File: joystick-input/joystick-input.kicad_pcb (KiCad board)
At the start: 2 copper layers, 53.3 x 39.4 mm, 11 parts

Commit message: joystick input rev 2 레이아웃팅
Signed-off-by: Ju, Gyeong-min <jcmh74@gmail.com>
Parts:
- removed H1, H2: MountingHole_Array_01x08_Pad, joystick-input:TestPoint_Bridge_Pitch5.08mm_Drill0.7mm_array_08_half
- removed OUT: Conn_01x05_Male, Connector_PinHeader_2.54mm:PinHeader_1x05_P2.54mm_Vertical
- added OUT1: Conn_01x05_Male, Connector_PinHeader_2.54mm:PinHeader_1x05_P2.54mm_Vertical, F.Cu at (162.1, 59.7)
- J1: renamed from JOYSTICK; value Conn_01x17_Male -> Conn_01x18_Male; footprint Connector_PinHeader_2.54mm:PinHeader_1x17_P2.54mm_Vertical -> Connector_PinHeader_2.54mm:PinHeader_1x18_P2.54mm_Vertical
- moved PULL1 10.9 mm to (141.2, 61.0)
- moved IN1 3.54 mm to (114.8, 59.7), turned to 180 degrees
- moved RN1 1.28 mm to (160.5, 40.0)
- moved RN2 1.28 mm to (116.3, 40.0)
- moved 74HC165_1 1.02 mm to (157.7, 49.5)
- moved 74HC165_2 0.51 mm to (136.7, 49.5)
- moved J1 0.51 mm to (160.0, 45.0)
- moved SHORT1 0.51 mm to (151.1, 61.1)
- renumbered IN to IN1, PULL to PULL1, SHORT to SHORT1
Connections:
- 74HC165_1 pad 11: /C_UP -> /C_B
- 74HC165_1 pad 12: /C_DOWN -> /C_A
- 74HC165_1 pad 13: /C_LEFT -> /C_SELECT
- 74HC165_1 pad 14: /C_RIGHT -> /C_START
- 74HC165_1 pad 3: /C_START -> /C_RIGHT
- 74HC165_1 pad 4: /C_SELECT -> /C_LEFT
- 74HC165_1 pad 5: /C_A -> /C_DOWN
- 74HC165_1 pad 6: /C_B -> /C_UP
- 74HC165_2 pad 11: /C_X -> /C_EX4
- 74HC165_2 pad 12: /C_Y -> /C_EX3
- 74HC165_2 pad 13: /C_L -> /C_EX2
- 74HC165_2 pad 14: /C_R -> /C_EX1
- 74HC165_2 pad 3: /C_EX1 -> /C_R
- 74HC165_2 pad 4: /C_EX2 -> /C_L
- 74HC165_2 pad 5: /C_EX3 -> /C_Y
- 74HC165_2 pad 6: /C_EX4 -> /C_X
- IN1 pad 3: /CLK -> /LOAD
- IN1 pad 4: /LOAD -> /CLK
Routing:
- net /PULL: track 82.0 -> 0.00 mm
- net VCC: track 73.8 -> 0.00 mm
- net /LOAD: track 60.7 -> 0.00 mm, vias 1 -> 0
- net /CLK: track 50.0 -> 0.00 mm, vias 1 -> 0
- net /C_UP: track 38.8 -> 0.00 mm
- net /C_Y: track 36.0 -> 0.00 mm
- net /C_X: track 32.2 -> 0.00 mm
- net /C_DOWN: track 31.7 -> 0.00 mm
- net /Q7: track 27.8 -> 0.00 mm
- net /C_RIGHT: track 25.0 -> 0.00 mm
- net /C_LEFT: track 25.0 -> 0.00 mm
- net /C_L: track 20.7 -> 0.00 mm, vias 1 -> 0
- net /C_R: track 19.7 -> 0.00 mm
- net /D_OUT: track 16.1 -> 0.00 mm
- net /C_SHORT: track 30.8 -> 45.4 mm
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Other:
- board size 53.3 x 39.4 mm -> 53.3 x 29.2 mm
- board text added: "Rev.2"
- board text added: "Short 16 15 14 13 12 11 10 9 8 7 6 5 4 3 2 1 Short"
- board text removed: "16 15 14 13 12 11 10 9 8 7 6 5 4 3 2 1 Short"
- board text removed: "Rev.1"

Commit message: 레이아웃 변경
Signed-off-by: Ju, Gyeong-min <jcmh74@gmail.com>
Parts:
- added C1: C, Capacitor_THT:C_Disc_D4.3mm_W1.9mm_P5.00mm, F.Cu at (157.7, 59.7)
- added C2: C, Capacitor_THT:C_Disc_D4.3mm_W1.9mm_P5.00mm, F.Cu at (136.7, 59.7)
- moved SHORT1 27.9 mm to (123.2, 60.5)
- moved PULL1 3.09 mm to (144.3, 60.5)
- moved IN1 0.25 mm to (114.8, 59.4)
- moved OUT1 0.25 mm to (162.1, 59.4)
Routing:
- net /PULL: track 0.00 -> 77.8 mm
- net VCC: track 0.00 -> 60.4 mm
- net /LOAD: track 0.00 -> 56.9 mm, vias 0 -> 2
- net /CLK: track 0.00 -> 55.4 mm, vias 0 -> 2
- net /D_OUT: track 0.00 -> 32.7 mm
- net /C_UP: track 0.00 -> 26.8 mm
- net /C_X: track 0.00 -> 26.5 mm
- net /Q7: track 0.00 -> 25.3 mm
- net /C_DOWN: track 0.00 -> 20.8 mm
- net /C_Y: track 0.00 -> 20.5 mm
- net /C_START: track 0.00 -> 19.6 mm
- net /C_SELECT: track 0.00 -> 19.6 mm
- net /C_B: track 0.00 -> 19.6 mm
- net /C_A: track 0.00 -> 19.6 mm
- net /C_SHORT: track 45.4 -> 64.6 mm
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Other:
- board text added: "V G LD CK D"
- board text added: "V G LD CK IN"
- board text removed: "V G CK LD D"
- board text removed: "V G CK LD IN"

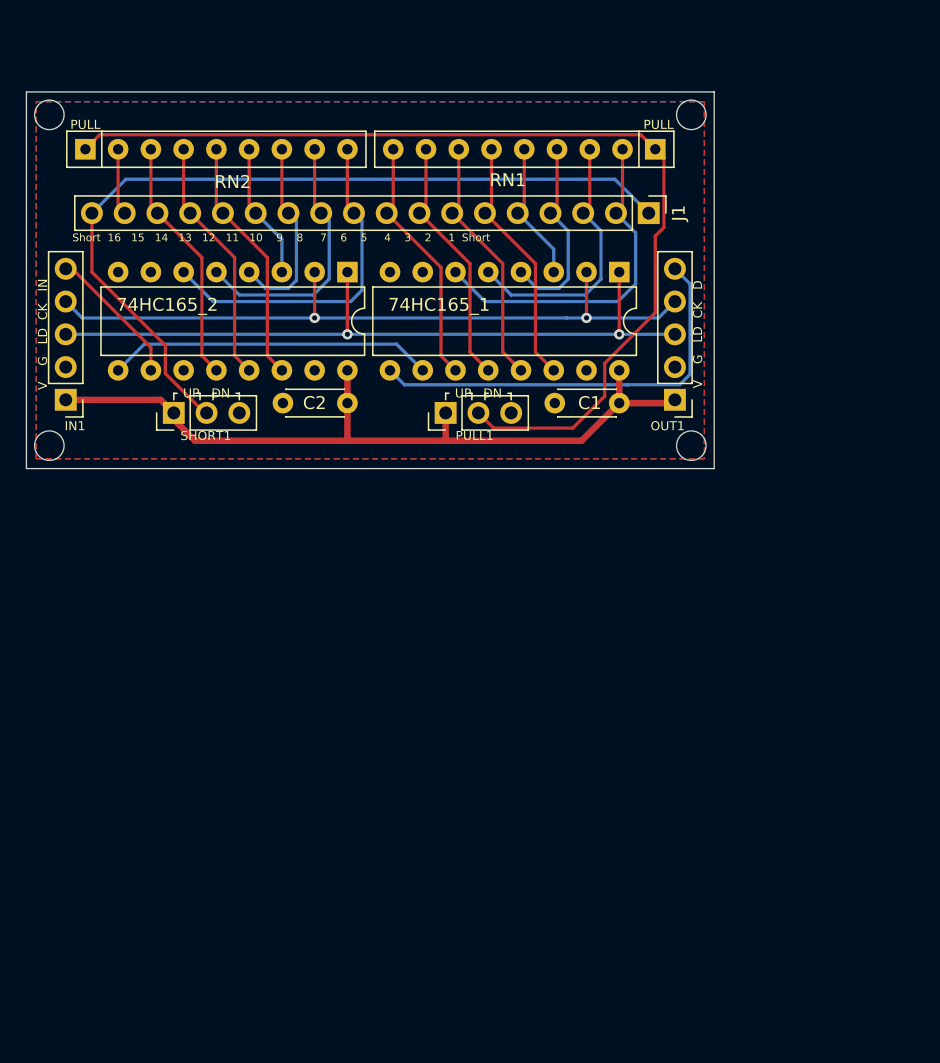
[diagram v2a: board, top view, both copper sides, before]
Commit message: joystick-input dip 버전 커넥터 위치 변경 & 점퍼 타입 변경
Signed-off-by: Ju, Gyeong-min <jcmh74@gmail.com>
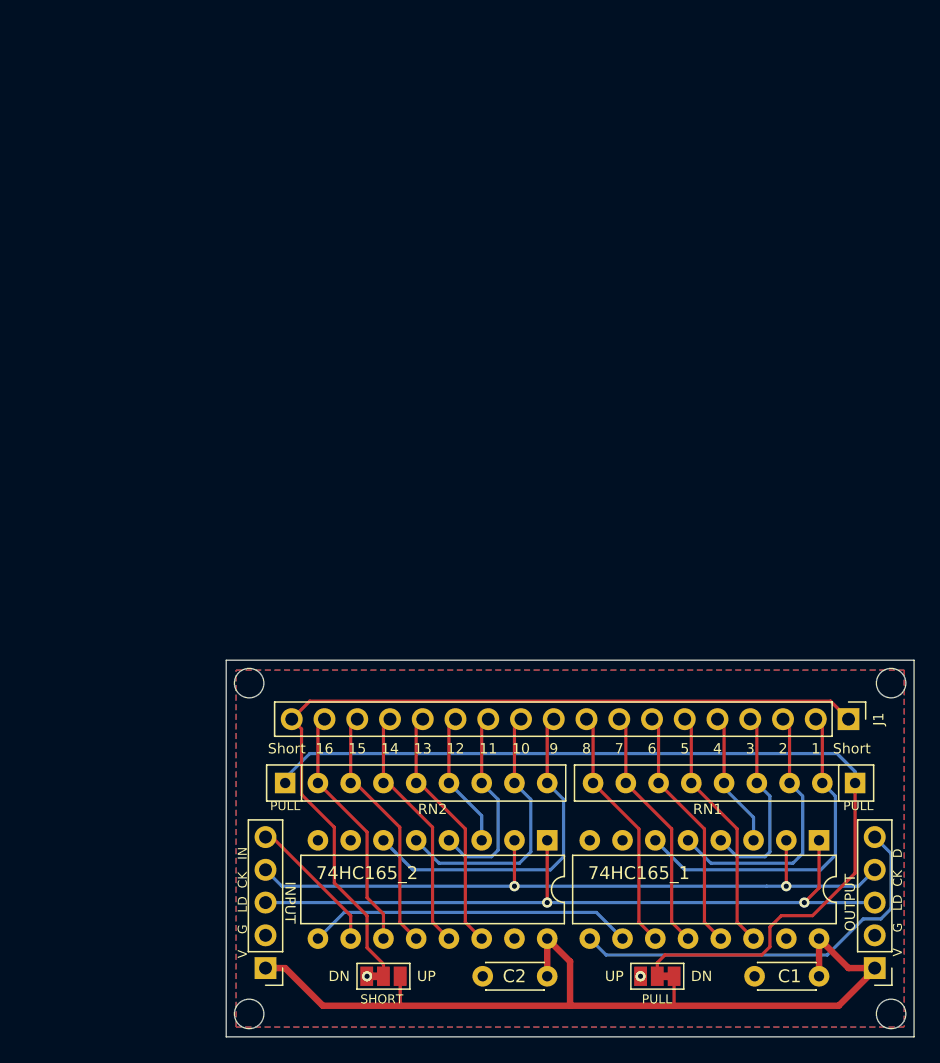
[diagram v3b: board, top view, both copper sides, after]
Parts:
- PULL1, SHORT1: footprint Connector_PinHeader_2.54mm:PinHeader_1x03_P2.54mm_Vertical -> Jumper:SolderJumper-3_P1.3mm_Bridged12_Pad1.0x1.5mm_NumberLabels
- moved RN1 51.5 mm to (176.0, 89.2)
- moved RN2 51.5 mm to (131.8, 89.2)
- moved C1 47.1 mm to (173.2, 104.1)
- moved C2 47.1 mm to (152.1, 104.1)
- moved 74HC165_1 46.7 mm to (173.2, 93.6)
- moved 74HC165_2 46.7 mm to (152.1, 93.6)
- moved IN1 46.7 mm to (130.3, 103.5)
- moved OUT1 46.7 mm to (177.5, 103.5)
- moved PULL1 46.7 mm to (160.7, 104.1), turned to 180 degrees
- moved SHORT1 46.6 mm to (139.4, 104.1), turned to 0 degrees
- moved J1 42.2 mm to (175.5, 84.2)
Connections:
- SHORT1 pad 1: VCC -> GND
- SHORT1 pad 3: GND -> VCC
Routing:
- net /C_EX4: track 5.16 -> 19.3 mm
- net VCC: track 60.4 -> 71.4 mm
- net /PULL: track 77.8 -> 74.2 mm
- net /C_SHORT: track 64.6 -> 67.2 mm
- net /D_OUT: track 32.7 -> 31.5 mm
- net GND: vias 0 -> 2
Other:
- board text added: "1"
- board text added: "10"
- board text added: "11"
- board text added: "12"
- board text added: "13"
- board text added: "14"
- board text added: "15"
- board text added: "16"
- board text added: "2"
- board text added: "3"
- board text added: "4"
- board text added: "5"
- board text added: "6"
- board text added: "7"
- board text added: "8"
- board text added: "9"
- board text added: "INPUT"
- board text added: "OUTPUT"
- board text added: "SHORT"
- board text added: "Short"
- board text removed: "Short 16 15 14 13 12 11 10 9 8 7 6 5 4 3 2 1 Short"
- board text removed: "UP DN"

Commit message: kicad 6로 마이그레이션
Signed-off-by: Ju, Gyeong-min <jcmh74@gmail.com>
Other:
- net class Default removed
- net class Power removed

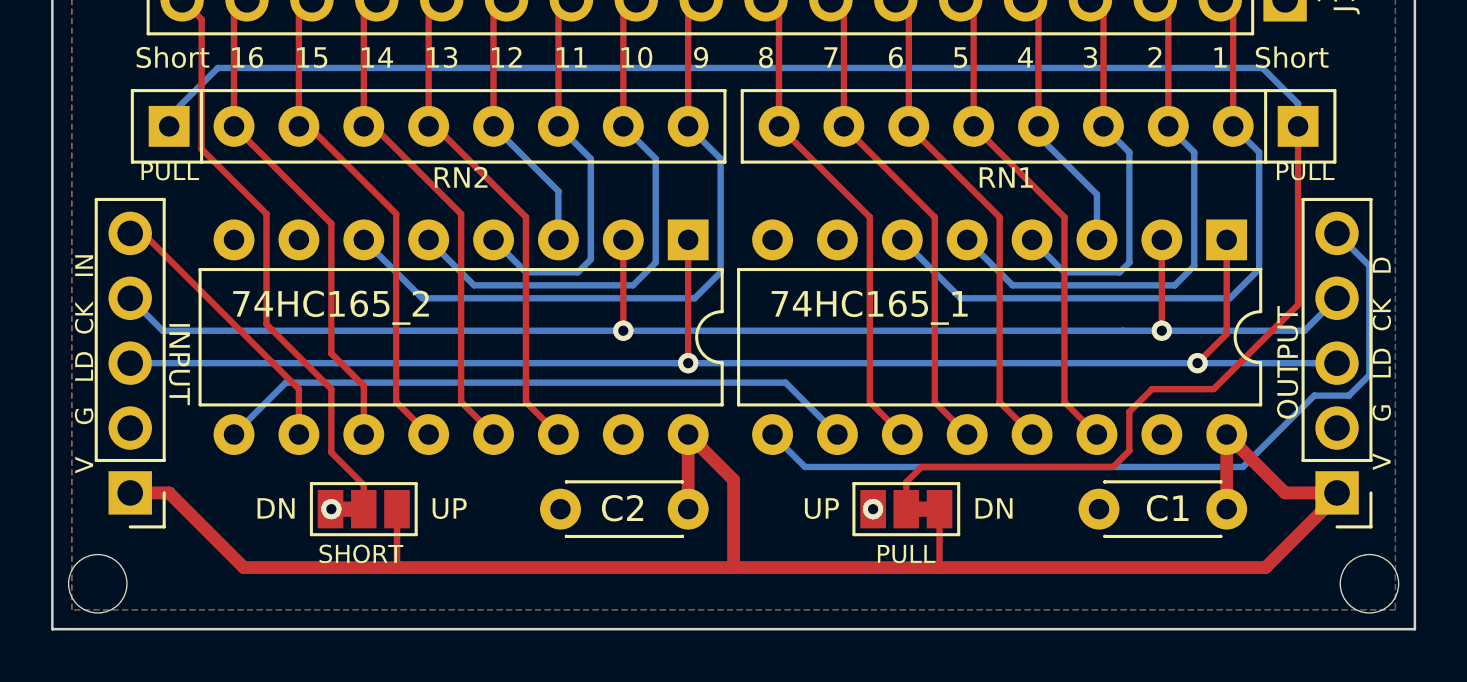
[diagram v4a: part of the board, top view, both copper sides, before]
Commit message: joystick-input 레이아웃 개선
Signed-off-by: Ju, Gyeong-min <jcmh74@gmail.com>
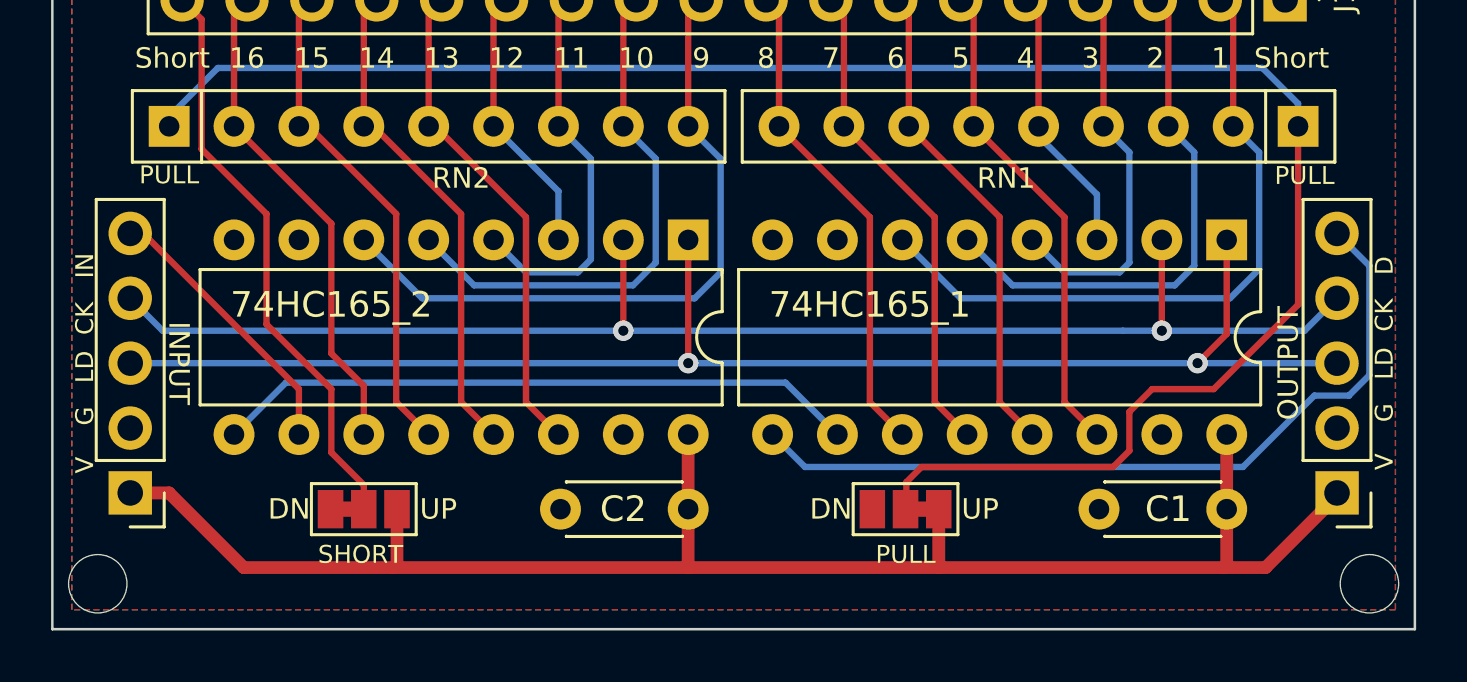
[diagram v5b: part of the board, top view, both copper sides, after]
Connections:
- 74HC165_1 pad 7: (no net) -> unconnected-(74HC165_1-Pad7)
- 74HC165_2 pad 7: (no net) -> unconnected-(74HC165_2-Pad7)
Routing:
- net VCC: track 71.4 -> 64.6 mm
- net GND: vias 2 -> 0
